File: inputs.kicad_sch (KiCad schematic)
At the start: 14 parts, among them J10 Conn_01x03, J20 Conn_01x03, J23 Conn_01x03, J26 Conn_01x03, U21 LTV-247, U22 LTV-247

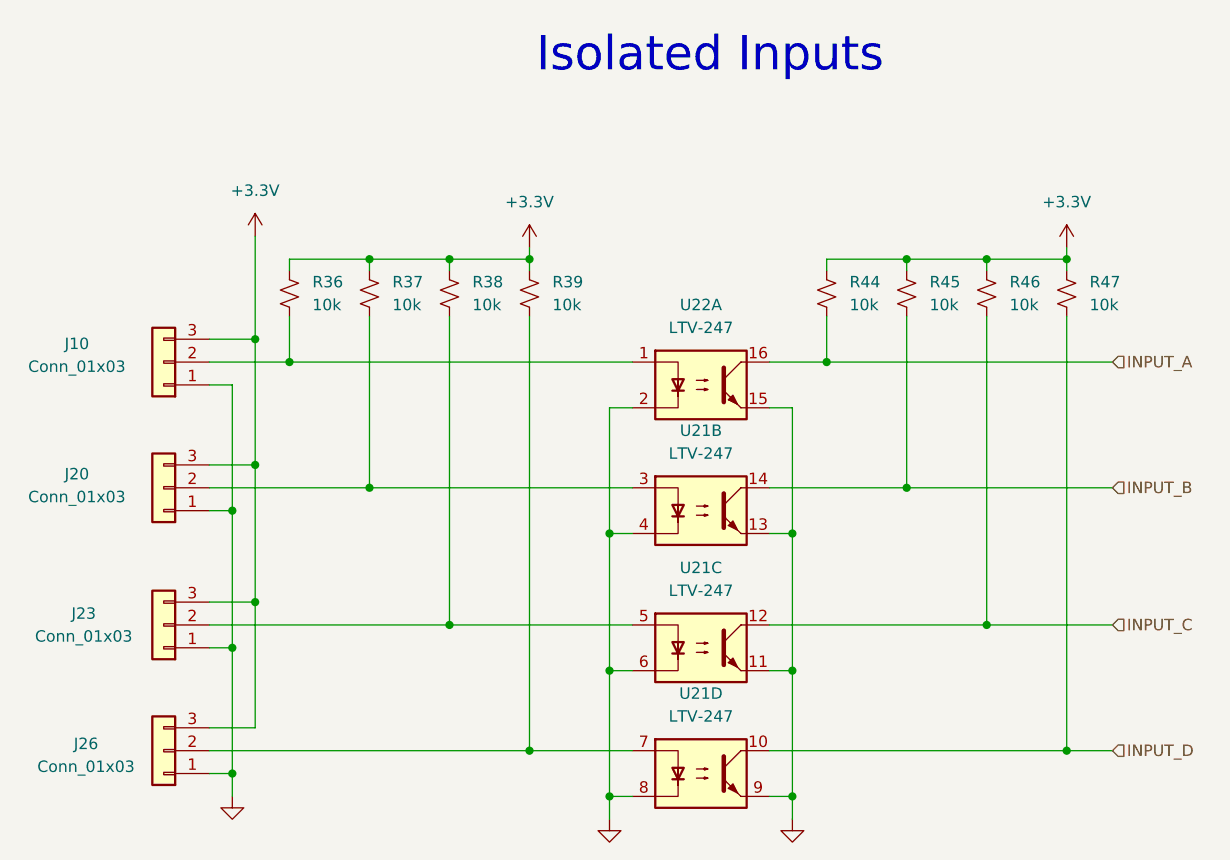
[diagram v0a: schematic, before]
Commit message: Soften scope, begin layout, reorganize sheets (still need to delete extras)
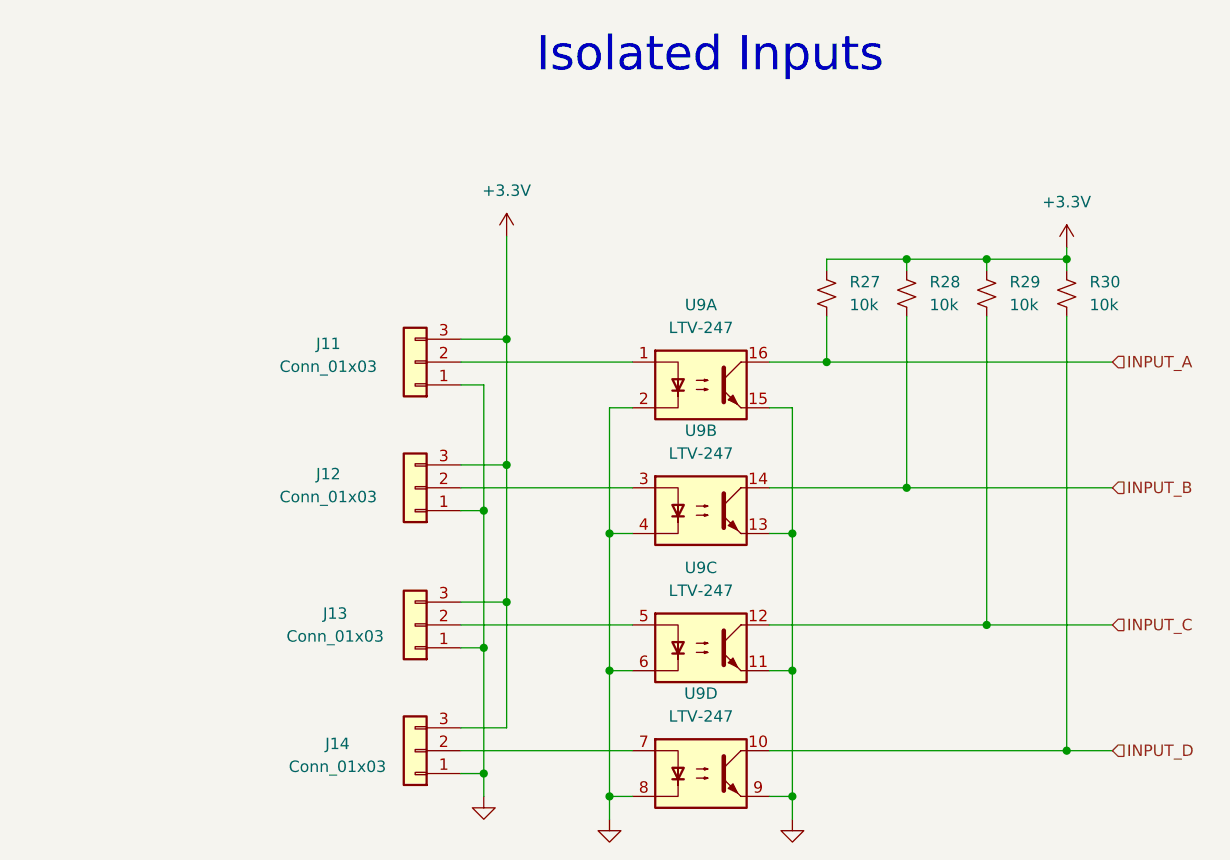
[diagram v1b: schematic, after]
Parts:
- removed R36, R37, R38, R39: 10k, symbol Device:R_Small_US
- J11: renamed from J10; footprint (none) -> Connector_Molex:Molex_Micro-Fit_3.0_43650-0315_1x03_P3.00mm_Vertical
- J12: renamed from J20; footprint (none) -> Connector_Molex:Molex_Micro-Fit_3.0_43650-0315_1x03_P3.00mm_Vertical
- J13: renamed from J23; footprint (none) -> Connector_Molex:Molex_Micro-Fit_3.0_43650-0315_1x03_P3.00mm_Vertical
- J14: renamed from J26; footprint (none) -> Connector_Molex:Molex_Micro-Fit_3.0_43650-0315_1x03_P3.00mm_Vertical
- R27: renamed from R44; footprint (none) -> APRLPrints:R_0603
- R28: renamed from R45; footprint (none) -> APRLPrints:R_0603
- R29: renamed from R46; footprint (none) -> APRLPrints:R_0603
- R30: renamed from R47; footprint (none) -> APRLPrints:R_0603
- renumbered U21 to U9, U22 to U9
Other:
- moved on the sheet: J11, J12, J13, J14

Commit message: ???
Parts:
- renumbered J11 to J19, J12 to J20, J13 to J21, J14 to J22, R27 to R50, R28 to R51, R29 to R52, R30 to R53, U9 to U20

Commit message: loadcell math coming soon(tm)
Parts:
- J18: renamed from J19; footprint Connector_Molex:Molex_Micro-Fit_3.0_43650-0315_1x03_P3.00mm_Vertical -> Connector_JST:JST_XH_B3B-XH-AM_1x03_P2.50mm_Vertical
- J19: renamed from J20; footprint Connector_Molex:Molex_Micro-Fit_3.0_43650-0315_1x03_P3.00mm_Vertical -> Connector_JST:JST_XH_B3B-XH-AM_1x03_P2.50mm_Vertical
- J20: renamed from J21; footprint Connector_Molex:Molex_Micro-Fit_3.0_43650-0315_1x03_P3.00mm_Vertical -> Connector_JST:JST_XH_B3B-XH-AM_1x03_P2.50mm_Vertical
- J21: renamed from J22; footprint Connector_Molex:Molex_Micro-Fit_3.0_43650-0315_1x03_P3.00mm_Vertical -> Connector_JST:JST_XH_B3B-XH-AM_1x03_P2.50mm_Vertical
- renumbered R50 to R62, R51 to R63, R52 to R64, R53 to R65, U20 to U18

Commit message: a
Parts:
- J14: renamed from J18; footprint Connector_JST:JST_XH_B3B-XH-AM_1x03_P2.50mm_Vertical -> libserie:JST_XH_B3B-XH-AM_1x03_P2.50mm_Vertical
- J15: renamed from J19; footprint Connector_JST:JST_XH_B3B-XH-AM_1x03_P2.50mm_Vertical -> libserie:JST_XH_B3B-XH-AM_1x03_P2.50mm_Vertical
- J16: renamed from J20; footprint Connector_JST:JST_XH_B3B-XH-AM_1x03_P2.50mm_Vertical -> libserie:JST_XH_B3B-XH-AM_1x03_P2.50mm_Vertical
- J17: renamed from J21; footprint Connector_JST:JST_XH_B3B-XH-AM_1x03_P2.50mm_Vertical -> libserie:JST_XH_B3B-XH-AM_1x03_P2.50mm_Vertical
- renumbered R62 to R61, R63 to R62, R64 to R63, R65 to R64, U18 to U20
